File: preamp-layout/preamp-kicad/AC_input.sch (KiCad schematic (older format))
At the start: 8 parts, among them J1 Conn_01x02_Female, J2 Screw_Terminal_01x03, J3 Screw_Terminal_01x03, J4 Screw_Terminal_01x03

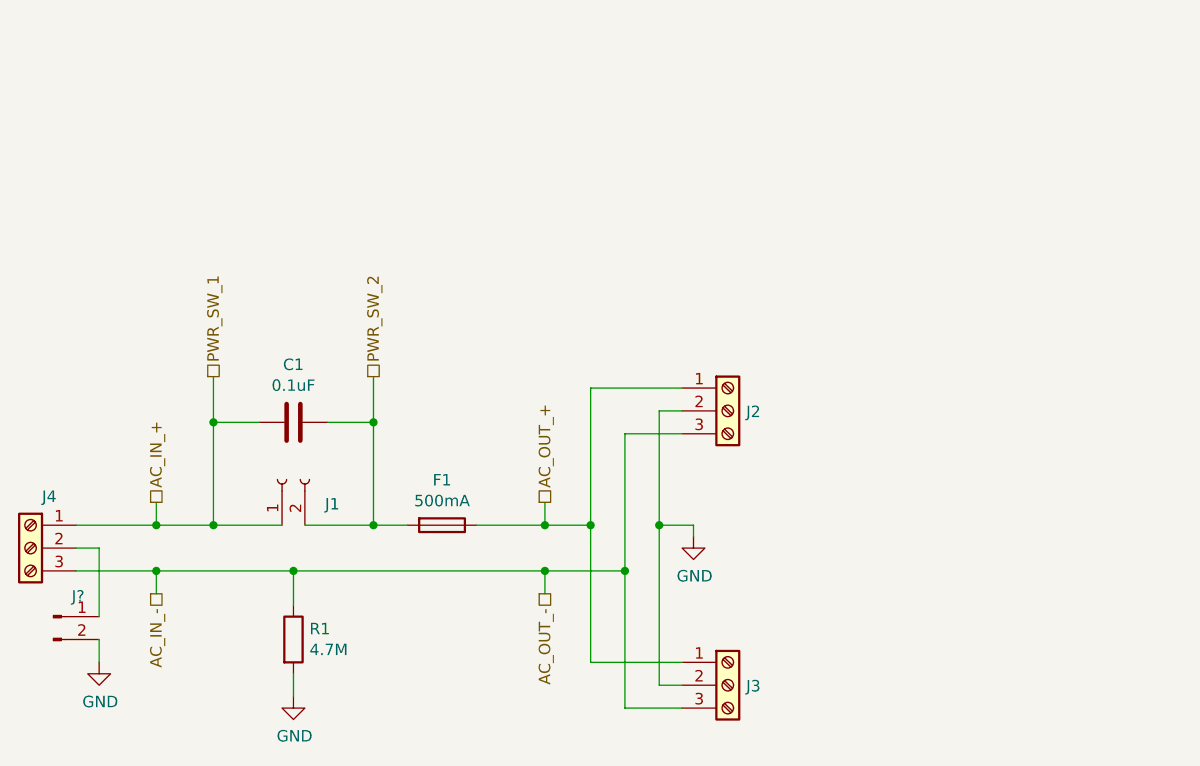
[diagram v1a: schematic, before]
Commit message: Incorporated Standby Relay
The Relay shown on the AC Input page is meant to control the +/-15V supply. The coil is controlled by two pins on the esp32 MCU. The 5V supply will be active at all times. I think the working condition will be something like, both pins are low then one goes high to move the switch, then goes back to low. when another state change happens the other pin will go high and move the switch back, etc.
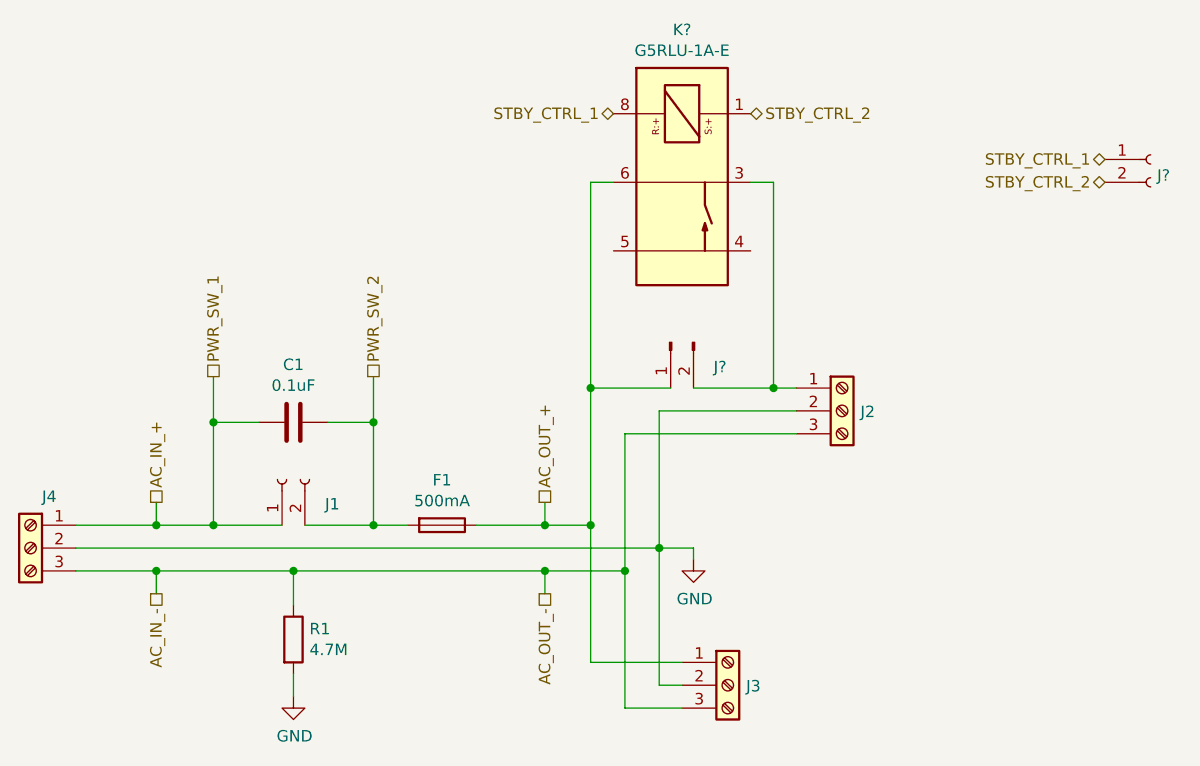
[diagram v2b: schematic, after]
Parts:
- removed J?: Conn_01x02_Male, Connector_JST:JST_EH_B2B-EH-A_1x02_P2.50mm_Vertical, symbol Connector:Conn_01x02_Male
- added J?: Conn_01x02_Female, Connector_JST:JST_EH_B2B-EH-A_1x02_P2.50mm_Vertical, symbol Connector:Conn_01x02_Female
- added J?: Conn_01x02_Male, Connector_JST:JST_EH_B2B-EH-A_1x02_P2.50mm_Vertical, symbol Connector:Conn_01x02_Male
- added K?: G5RLU-1A-E, symbol preamp:G5RLU-1A-E
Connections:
- net AC_OUT_+: now also J?.1 (Pin_1), K?.6; no longer J2.1 (Pin_1)
- net GND: now also J4.2 (Pin_2)
- new net: J2.1 (Pin_1), J?.2 (Pin_2), K?.3
- new net STBY_CTRL_1: J?.1 (Pin_1), K?.8
- new net STBY_CTRL_2: J?.2 (Pin_2), K?.1
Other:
- moved on the sheet: J2
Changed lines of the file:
@@
 EESchema Schematic File Version 4
-LIBS:preamp-cache
 EELAYER 30 0
 EELAYER END
@@
 Wire Wire Line
 	4500 3850 4850 3850
-Wire Wire Line
-	4500 3950 4600 3950
-Wire Wire Line
-	4600 3950 4600 4250
 Connection ~ 4850 4050
 Wire Wire Line
@@
 Wire Wire Line
 	4850 3850 5100 3850
-$Comp
-L Connector:Conn_01x02_Male J?
-U 1 1 5F12D3AA
-P 4400 4250
-AR Path="/5E5EF2D4/5F12D3AA" Ref="J?"  Part="1"
-AR Path="/5E26F6FE/5F12D3AA" Ref="J?"  Part="1"
-F 0 "J?" H 4508 4339 50  0000 C CNN
-F 1 "Conn_01x02_Male" H 4372 4133 50  0001 R CNN
-F 2 "Connector_JST:JST_EH_B2B-EH-A_1x02_P2.50mm_Vertical" H 4400 4250 50  0001 C CNN
-F 3 "~" H 4400 4250 50  0001 C CNN
-	1    4400 4250
-	1    0    0    -1
-$EndComp
-$Comp
-L power:GND #PWR0111
-U 1 1 5E8D595F
-P 4600 4450
-F 0 "#PWR0111" H 4600 4200 50  0001 C CNN
-F 1 "GND" H 4605 4277 50  0000 C CNN
-F 2 "" H 4600 4450 50  0001 C CNN
-F 3 "" H 4600 4450 50  0001 C CNN
-	1    4600 4450
-	1    0    0    -1
-$EndComp
 Connection ~ 6550 4050
 Connection ~ 6550 3850
-Wire Wire Line
-	7050 3850 7050 4550
-Wire Wire Line
-	6750 3850 6750 4450
 Connection ~ 6900 4050
 Wire Wire Line
@@
 	6750 4450 7150 4450
 Wire Wire Line
-	7050 3350 7050 3850
-Wire Wire Line
 	6900 3450 6900 4050
 Wire Wire Line
-	6750 3250 6750 3850
-Connection ~ 7050 3850
-Wire Wire Line
-	7200 3850 7050 3850
-Wire Wire Line
-	7200 3900 7200 3850
+	7200 3950 7050 3950
+Wire Wire Line
+	7200 4000 7200 3950
 $Comp
 L power:GND #PWR0110
 U 1 1 5E8C517A
-P 7200 3900
-F 0 "#PWR0110" H 7200 3650 50  0001 C CNN
-F 1 "GND" H 7205 3727 50  0000 C CNN
-F 2 "" H 7200 3900 50  0001 C CNN
-F 3 "" H 7200 3900 50  0001 C CNN
-	1    7200 3900
+P 7200 4000
+F 0 "#PWR0110" H 7200 3750 50  0001 C CNN
+F 1 "GND" H 7205 3827 50  0000 C CNN
+F 2 "" H 7200 4000 50  0001 C CNN
+F 3 "" H 7200 4000 50  0001 C CNN
+	1    7200 4000
 	1    0    0    -1
 $EndComp
 Wire Wire Line
 	7050 4550 7150 4550
-Wire Wire Line
-	7150 3350 7050 3350
 $Comp
 L Connector:Screw_Terminal_01x03 J3
@@
 L Connector:Screw_Terminal_01x03 J2
 U 1 1 5E8BEBC3
-P 7350 3350
-F 0 "J2" H 7430 3346 50  0000 L CNN
-F 1 "Screw_Terminal_01x03" H 7268 3116 50  0001 C CNN
-F 2 "TerminalBlock_Phoenix:TerminalBlock_Phoenix_MKDS-3-3-5.08_1x03_P5.08mm_Horizontal" H 7350 3350 50  0001 C CNN
-F 3 "~" H 7350 3350 50  0001 C CNN
-	1    7350 3350
+P 7850 3350
+F 0 "J2" H 7930 3346 50  0000 L CNN
+F 1 "Screw_Terminal_01x03" H 7768 3116 50  0001 C CNN
+F 2 "TerminalBlock_Phoenix:TerminalBlock_Phoenix_MKDS-3-3-5.08_1x03_P5.08mm_Horizontal" H 7850 3350 50  0001 C CNN
+F 3 "~" H 7850 3350 50  0001 C CNN
+	1    7850 3350
 	1    0    0    -1
 $EndComp
 Wire Wire Line
 	6900 4650 7150 4650
+Wire Wire Line
+	6550 4050 6900 4050
+Wire Wire Line
+	6550 3850 6750 3850
+Wire Wire Line
+	4500 3950 7050 3950
+Connection ~ 7050 3950
+Wire Wire Line
+	7050 3950 7050 4550
+Wire Wire Line
+	7050 3350 7050 3950
+Wire Wire Line
+	6900 3450 7650 3450
+Wire Wire Line
+	7050 3350 7650 3350
+Wire Wire Line
+	7550 3250 7650 3250
+$Comp
+L Connector:Conn_01x02_Female J?
+U 1 1 5E5E0EF2
+P 9200 2250
+F 0 "J?" H 9228 2180 50  0000 L CNN
+F 1 "Conn_01x02_Female" V 9047 2062 50  0001 R CNN
+F 2 "Connector_JST:JST_EH_B2B-EH-A_1x02_P2.50mm_Vertical" H 9200 2250 50  0001 C CNN
+F 3 "~" H 9200 2250 50  0001 C CNN
+	1    9200 2250
+	1    0    0    -1
+$EndComp
+Text HLabel 9000 2350 0    50   BiDi ~ 0
+STBY_CTRL_2
+Text HLabel 9000 2250 0    50   BiDi ~ 0
+STBY_CTRL_1
+Wire Wire Line
+	6750 3850 6750 4450
+Text HLabel 7450 2050 2    50   BiDi ~ 0
+STBY_CTRL_2
+Text HLabel 6850 2050 0    50   BiDi ~ 0
+STBY_CTRL_1
+Wire Wire Line
+	6750 2350 6850 2350
+Wire Wire Line
+	7450 2350 7550 2350
+$Comp
+L preamp:G5RLU-1A-E K?
+U 1 1 5E5D8616
+P 7150 2350
+F 0 "K?" H 7150 3017 50  0000 C CNN
+F 1 "G5RLU-1A-E" H 7150 2926 50  0000 C CNN
+F 2 "" H 7150 1800 50  0001 C CNN
+F 3 "" H 7150 1800 50  0001 C CNN
+	1    7150 2350
+	1    0    0    -1
+$EndComp
+$Comp
+L Connector:Conn_01x02_Male J?
+U 1 1 5E605BF1
+P 7100 3050
+AR Path="/5E2D8DA2/5E605BF1" Ref="J?"  Part="1"
+AR Path="/5E26F6FE/5E605BF1" Ref="J?"  Part="1"
+F 0 "J?" V 7208 2862 50  0000 R CNN
+F 1 "Conn_01x02_Male" H 7072 2933 50  0001 R CNN
+F 2 "Connector_JST:JST_EH_B2B-EH-A_1x02_P2.50mm_Vertical" H 7100 3050 50  0001 C CNN
+F 3 "~" H 7100 3050 50  0001 C CNN
+	1    7100 3050
+	0    -1   1    0
+$EndComp
 Connection ~ 6750 3850
 Wire Wire Line
-	6550 4050 6900 4050
-Wire Wire Line
-	6550 3850 6750 3850
-Wire Wire Line
-	6900 3450 7150 3450
-Wire Wire Line
-	6750 3250 7150 3250
-Wire Wire Line
-	4600 4350 4600 4450
+	7100 3250 6750 3250
+Wire Wire Line
+	7200 3250 7550 3250
+Connection ~ 6750 3250
+Wire Wire Line
+	6750 3250 6750 3850
+Connection ~ 7550 3250
+Wire Wire Line
+	7550 2350 7550 3250
+Wire Wire Line
+	6750 2350 6750 3250
 $EndSCHEMATC

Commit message: BOM Update
parts added to BOM, connector cleanup. Stopping point before renumbering refdes in a more intelligent way.
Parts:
- gave numbers to parts that had none: 3
- renumbered J4 to J2, J1 to J3, J3 to J5, J2 to J7
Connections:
- net at J4.2 (Pin_2), J7.1 (Pin_1): now also K1.4; no longer K1.3
- no-connect marks 0 -> 2
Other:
- moved on the sheet: J6
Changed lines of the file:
@@
 Connection ~ 5100 3850
 $Comp
-L power:GND #PWR03
+L power:GND #PWR04
 U 1 1 649E3EA1
 P 5450 4600
-F 0 "#PWR03" H 5450 4350 50  0001 C CNN
+F 0 "#PWR04" H 5450 4350 50  0001 C CNN
 F 1 "GND" H 5455 4427 50  0000 C CNN
 F 2 "" H 5450 4600 50  0001 C CNN
@@
 $EndComp
 $Comp
-L Connector:Conn_01x02_Female J1
+L Connector:Conn_01x02_Female J3
 U 1 1 5E2B212C
 P 5400 3650
-F 0 "J1" V 5292 3462 50  0000 R CNN
+F 0 "J3" V 5292 3462 50  0000 R CNN
 F 1 "Conn_01x02_Female" V 5247 3462 50  0001 R CNN
 F 2 "Connector_JST:JST_EH_B2B-EH-A_1x02_P2.50mm_Vertical" H 5400 3650 50  0001 C CNN
@@
 	4850 4150 4850 4050
 $Comp
-L Connector:Screw_Terminal_01x03 J4
+L Connector:Screw_Terminal_01x03 J2
 U 1 1 5E8BB7CA
 P 4300 3950
-F 0 "J4" H 4218 4175 50  0000 C CNN
+F 0 "J2" H 4218 4175 50  0000 C CNN
 F 1 "Screw_Terminal_01x03" H 4218 3716 50  0001 C CNN
 F 2 "TerminalBlock_Phoenix:TerminalBlock_Phoenix_MKDS-3-3-5.08_1x03_P5.08mm_Horizontal" H 4300 3950 50  0001 C CNN
@@
 	7200 4000 7200 3950
 $Comp
-L power:GND #PWR0110
+L power:GND #PWR05
 U 1 1 5E8C517A
 P 7200 4000
-F 0 "#PWR0110" H 7200 3750 50  0001 C CNN
+F 0 "#PWR05" H 7200 3750 50  0001 C CNN
 F 1 "GND" H 7205 3827 50  0000 C CNN
 F 2 "" H 7200 4000 50  0001 C CNN
@@
 	7050 4550 7150 4550
 $Comp
-L Connector:Screw_Terminal_01x03 J3
+L Connector:Screw_Terminal_01x03 J5
 U 1 1 5E8C1BA2
 P 7350 4550
-F 0 "J3" H 7430 4546 50  0000 L CNN
+F 0 "J5" H 7430 4546 50  0000 L CNN
 F 1 "Screw_Terminal_01x03" H 7268 4316 50  0001 C CNN
 F 2 "TerminalBlock_Phoenix:TerminalBlock_Phoenix_MKDS-3-3-5.08_1x03_P5.08mm_Horizontal" H 7350 4550 50  0001 C CNN
@@
 $EndComp
 $Comp
-L Connector:Screw_Terminal_01x03 J2
+L Connector:Screw_Terminal_01x03 J7
 U 1 1 5E8BEBC3
 P 7850 3350
-F 0 "J2" H 7930 3346 50  0000 L CNN
+F 0 "J7" H 7930 3346 50  0000 L CNN
 F 1 "Screw_Terminal_01x03" H 7768 3116 50  0001 C CNN
 F 2 "TerminalBlock_Phoenix:TerminalBlock_Phoenix_MKDS-3-3-5.08_1x03_P5.08mm_Horizontal" H 7850 3350 50  0001 C CNN
@@
 Wire Wire Line
 	7050 3350 7650 3350
-Wire Wire Line
-	7550 3250 7650 3250
-$Comp
-L Connector:Conn_01x02_Female J?
+$Comp
+L Connector:Conn_01x02_Female J6
 U 1 1 5E5E0EF2
-P 9200 2250
-F 0 "J?" H 9228 2180 50  0000 L CNN
-F 1 "Conn_01x02_Female" V 9047 2062 50  0001 R CNN
-F 2 "Connector_JST:JST_EH_B2B-EH-A_1x02_P2.50mm_Vertical" H 9200 2250 50  0001 C CNN
-F 3 "~" H 9200 2250 50  0001 C CNN
-	1    9200 2250
-	1    0    0    -1
-$EndComp
-Text HLabel 9000 2350 0    50   BiDi ~ 0
+P 7550 1300
+F 0 "J6" H 7578 1230 50  0000 L CNN
+F 1 "Conn_01x02_Female" V 7397 1112 50  0001 R CNN
+F 2 "Connector_JST:JST_EH_B2B-EH-A_1x02_P2.50mm_Vertical" H 7550 1300 50  0001 C CNN
+F 3 "~" H 7550 1300 50  0001 C CNN
+	1    7550 1300
+	1    0    0    -1
+$EndComp
+Text HLabel 7350 1400 0    50   BiDi ~ 0
 STBY_CTRL_2
-Text HLabel 9000 2250 0    50   BiDi ~ 0
+Text HLabel 7350 1300 0    50   BiDi ~ 0
 STBY_CTRL_1
 Wire Wire Line
@@
 Wire Wire Line
 	6750 2350 6850 2350
-Wire Wire Line
-	7450 2350 7550 2350
-$Comp
-L preamp:G5RLU-1A-E K?
+$Comp
+L preamp:G5RLU-1A-E K1
 U 1 1 5E5D8616
 P 7150 2350
-F 0 "K?" H 7150 3017 50  0000 C CNN
+F 0 "K1" H 7150 3017 50  0000 C CNN
 F 1 "G5RLU-1A-E" H 7150 2926 50  0000 C CNN
 F 2 "" H 7150 1800 50  0001 C CNN
@@
 P 7100 3050
 AR Path="/5E2D8DA2/5E605BF1" Ref="J?"  Part="1"
-AR Path="/5E26F6FE/5E605BF1" Ref="J?"  Part="1"
-F 0 "J?" V 7208 2862 50  0000 R CNN
+AR Path="/5E26F6FE/5E605BF1" Ref="J4"  Part="1"
+F 0 "J4" V 7208 2862 50  0000 R CNN
 F 1 "Conn_01x02_Male" H 7072 2933 50  0001 R CNN
 F 2 "Connector_JST:JST_EH_B2B-EH-A_1x02_P2.50mm_Vertical" H 7100 3050 50  0001 C CNN
@@
 Wire Wire Line
 	7100 3250 6750 3250
+Connection ~ 6750 3250
+Wire Wire Line
+	6750 3250 6750 3850
+Wire Wire Line
+	6750 2350 6750 3250
 Wire Wire Line
 	7200 3250 7550 3250
-Connection ~ 6750 3250
-Wire Wire Line
-	6750 3250 6750 3850
+Wire Wire Line
+	7450 2650 7550 2650
+Wire Wire Line
+	7550 2650 7550 3250
 Connection ~ 7550 3250
 Wire Wire Line
-	7550 2350 7550 3250
-Wire Wire Line
-	6750 2350 6750 3250
+	7550 3250 7650 3250
+NoConn ~ 7450 2350
+NoConn ~ 6850 2650
 $EndSCHEMATC

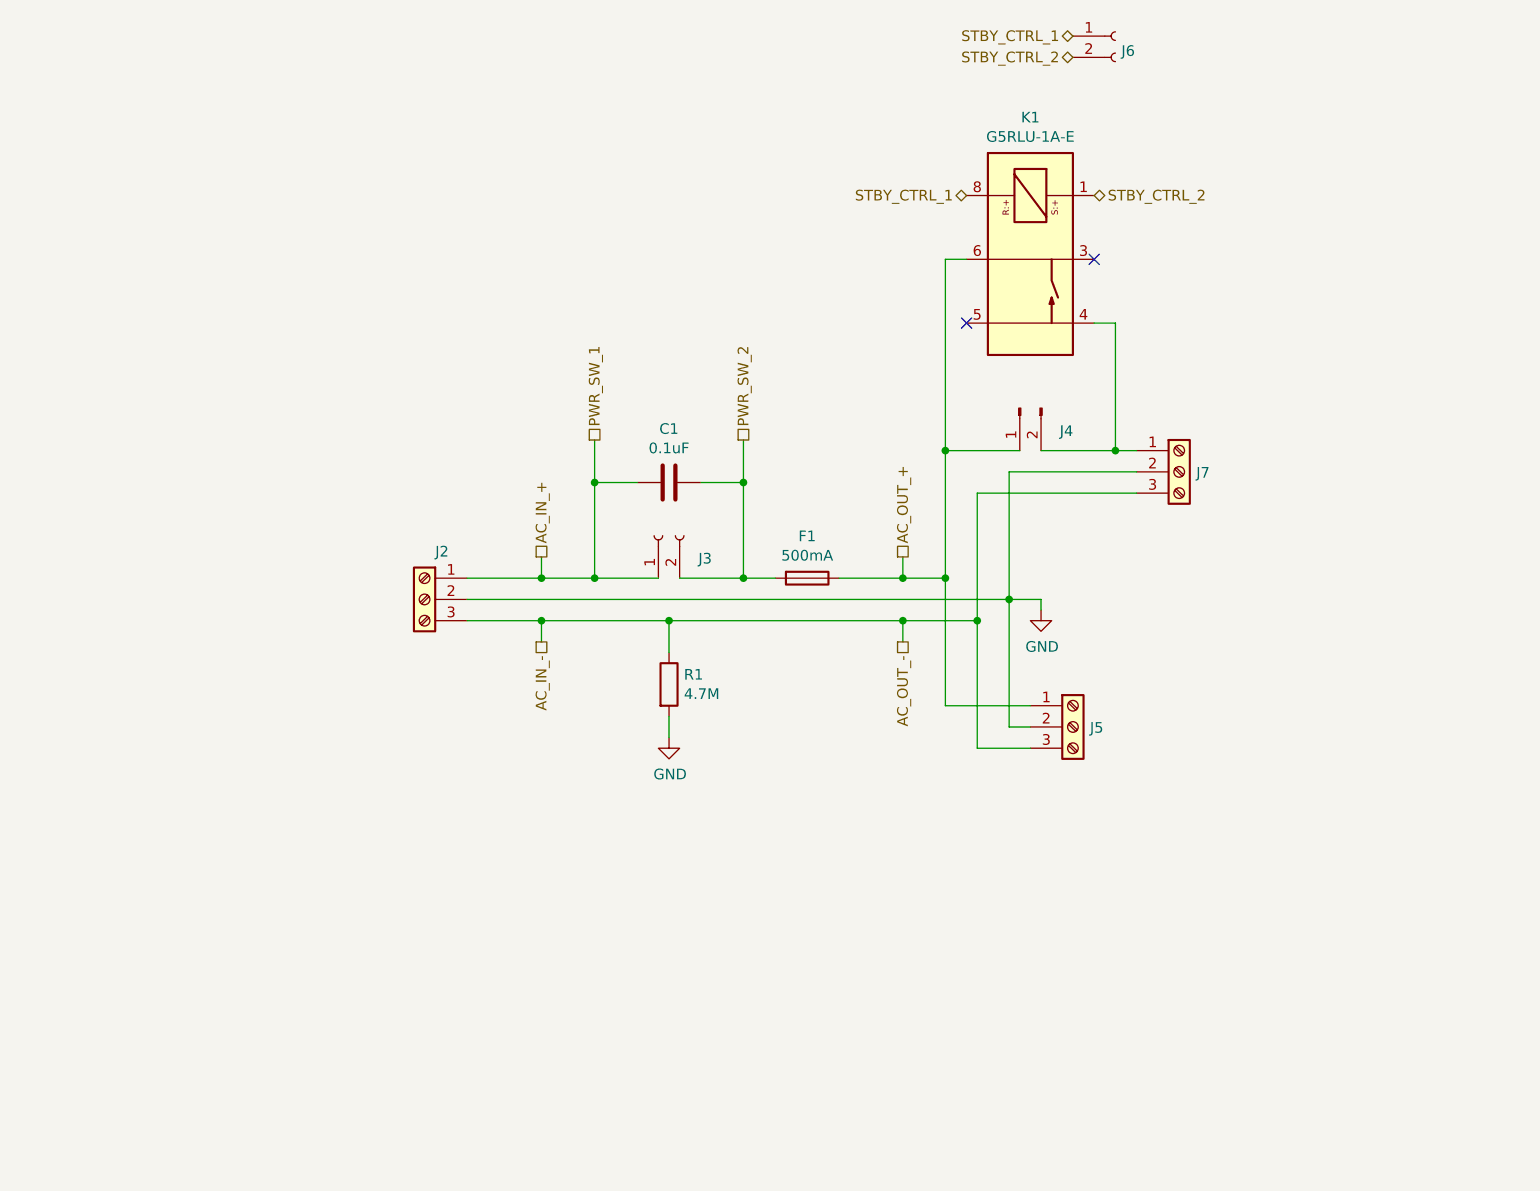
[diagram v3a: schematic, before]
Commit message: Power Supply Update
Grounding made more clear, tied to chassis on AC board. Pins renamed. Aligned with AC wall power convention. General cleanup.
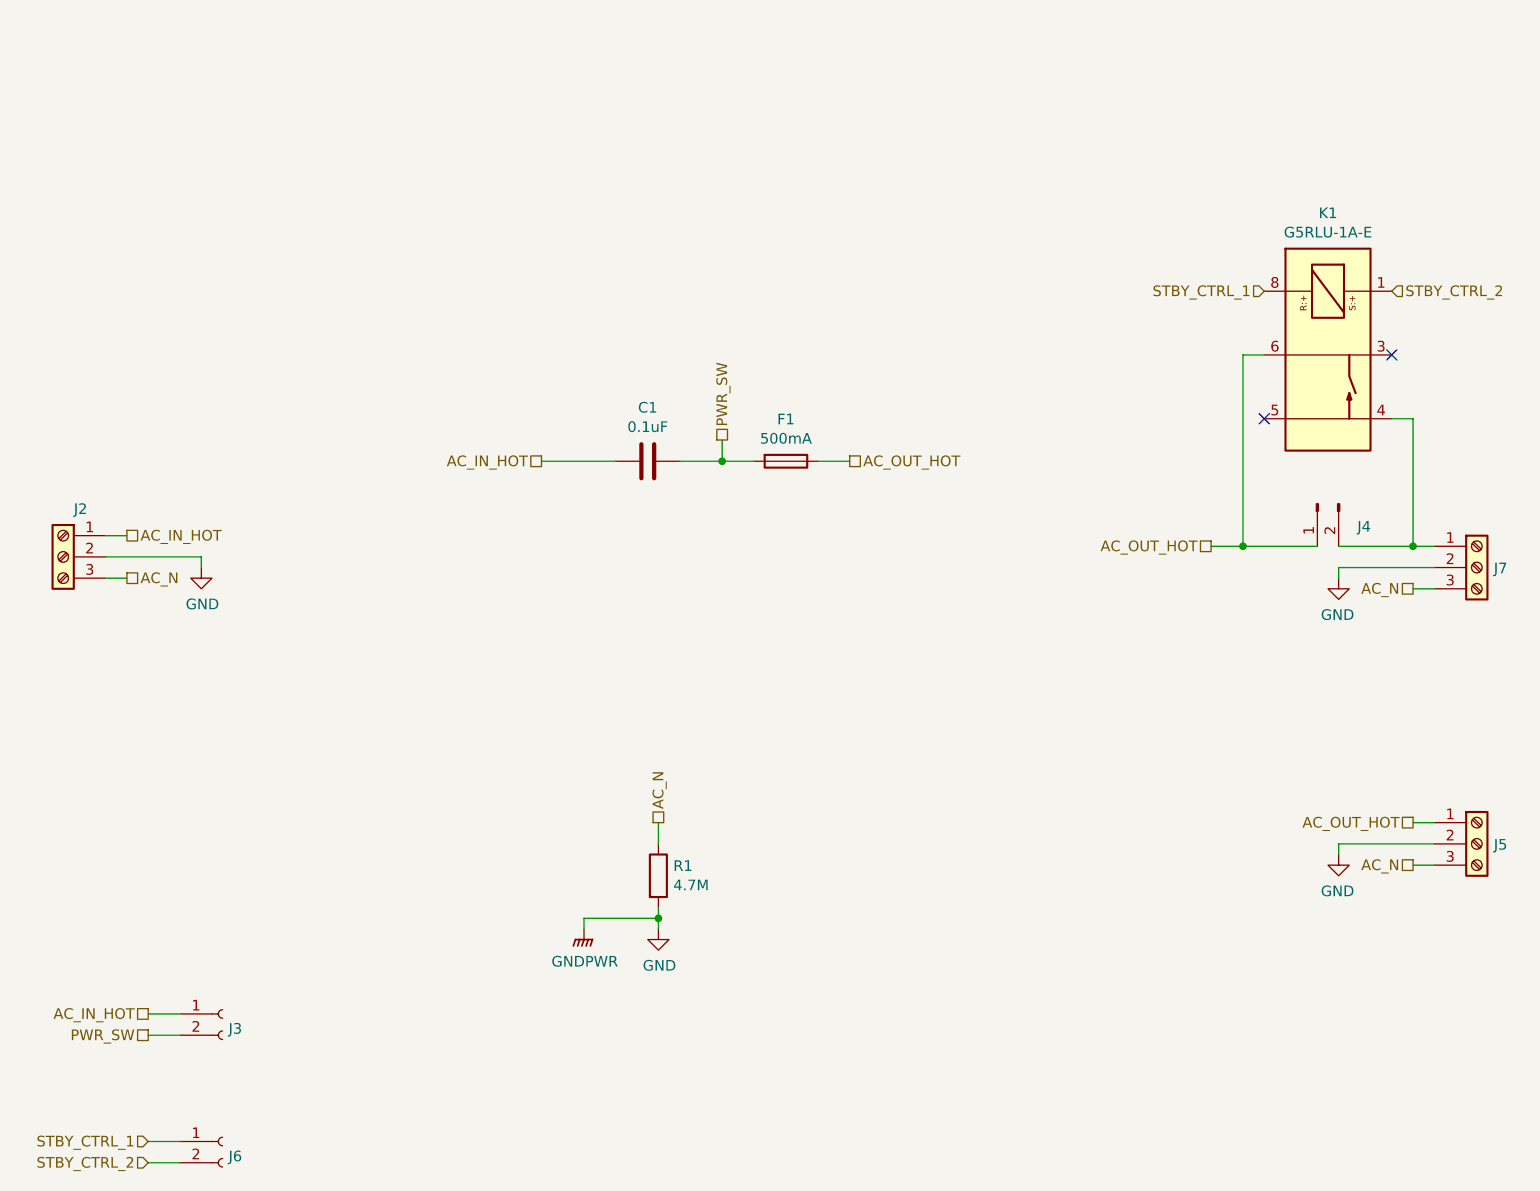
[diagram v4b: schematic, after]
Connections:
- net AC_IN_+ renamed AC_IN_HOT
- net AC_IN_- renamed AC_N
- net AC_OUT_+ renamed AC_OUT_HOT
- net PWR_SW_2 renamed PWR_SW
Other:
- moved on the sheet: C1, F1, J2, J3, J4, J5, J6, J7, K1, R1
